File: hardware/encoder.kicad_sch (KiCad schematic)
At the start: 9 parts, among them SW2 PEC12R Encoder

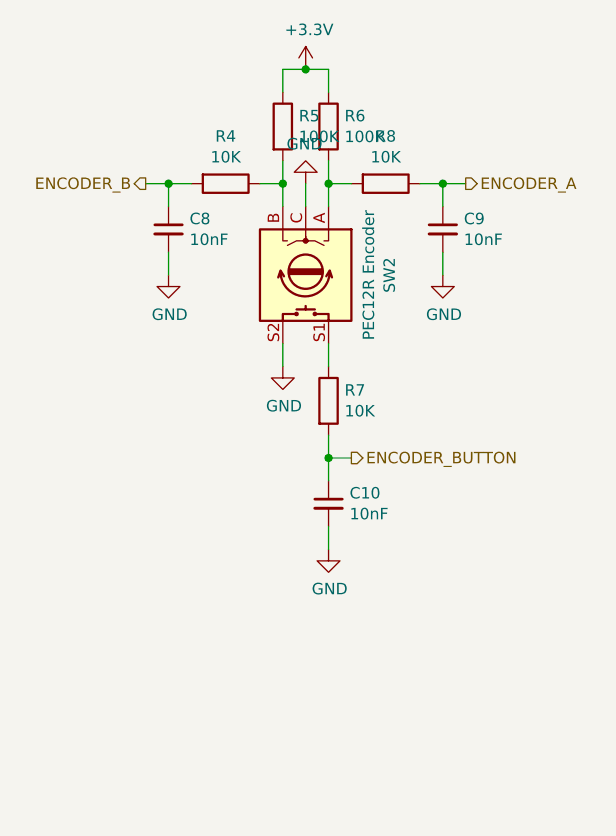
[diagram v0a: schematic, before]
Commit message: Updated schematic according to reference design
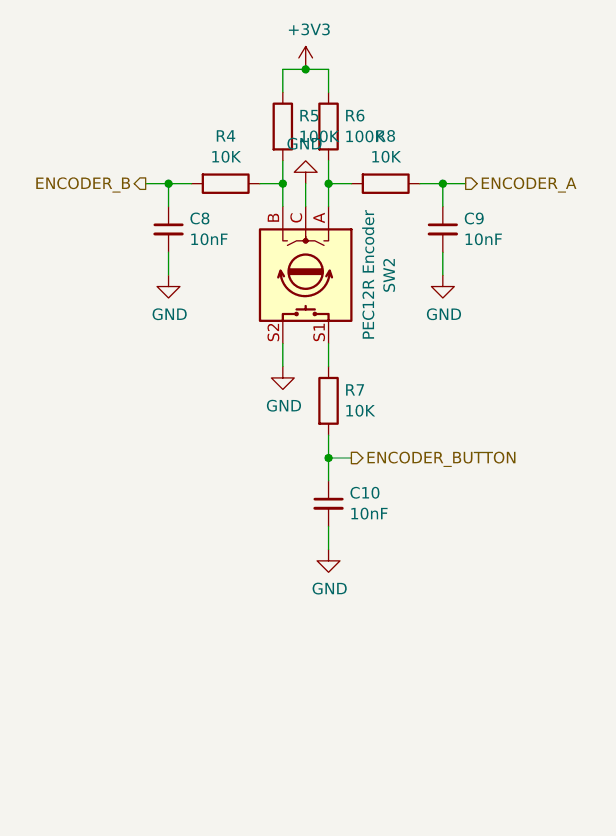
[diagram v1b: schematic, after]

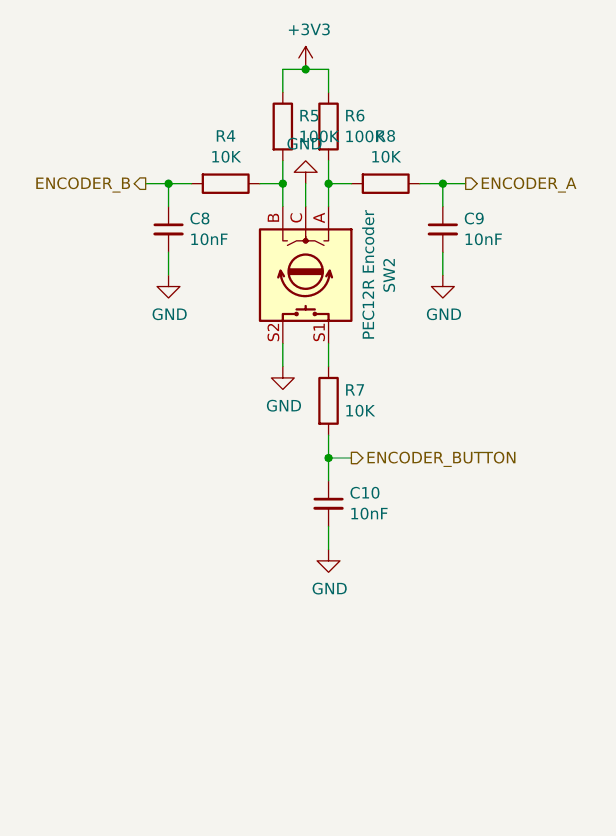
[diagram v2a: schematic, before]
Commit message: Regenerated reference designators, changed to rail-to-rail op-amps
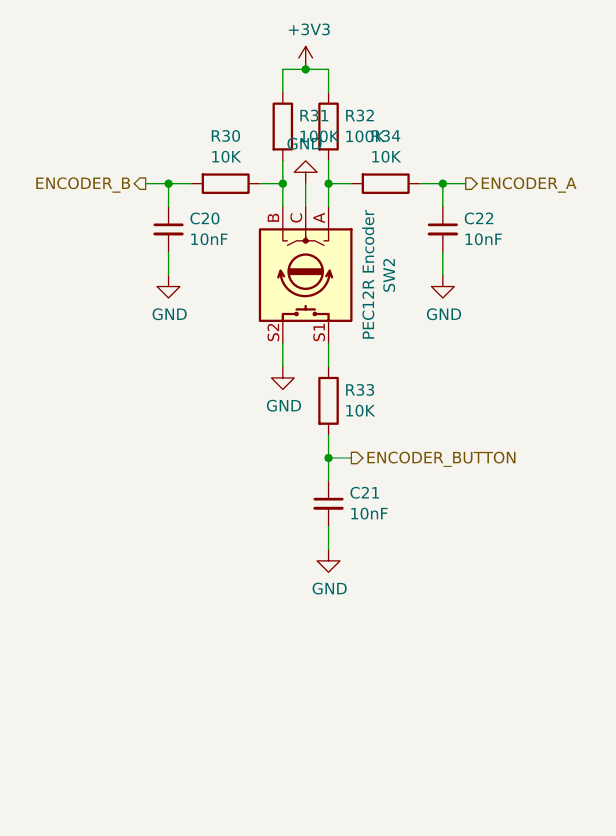
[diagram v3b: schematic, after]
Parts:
- renumbered C8 to C20, C10 to C21, C9 to C22, R4 to R30, R5 to R31, R6 to R32, R7 to R33, R8 to R34
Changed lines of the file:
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@@
 		(on_board yes)
 		(dnp no)
-		(property "Reference" "#PWR0109"
+		(property "Reference" "#PWR061"
 			(at 109.22 50.8 0)
 			(effects
@@
 			(project ""
 				(path "/adf38c8f-bada-4838-acc6-e6af19946742/82306041-d571-45f1-89c8-d149d0eff0c6"
-					(reference "#PWR0109")
+					(reference "#PWR061")
 					(unit 1)
 				)
@@
 		(on_board yes)
 		(dnp no)
-		(property "Reference" "R5"
+		(property "Reference" "R31"
 			(at 108.458 52.1716 0)
 			(effects
@@
 			(project ""
 				(path "/adf38c8f-bada-4838-acc6-e6af19946742/82306041-d571-45f1-89c8-d149d0eff0c6"
-					(reference "R5")
+					(reference "R31")
 					(unit 1)
 				)
@@
 		(on_board yes)
 		(dnp no)
-		(property "Reference" "R4"
+		(property "Reference" "R30"
 			(at 100.33 54.4322 90)
 			(effects
@@
 			(project ""
 				(path "/adf38c8f-bada-4838-acc6-e6af19946742/82306041-d571-45f1-89c8-d149d0eff0c6"
-					(reference "R4")
+					(reference "R30")
 					(unit 1)
 				)
@@
 		(on_board yes)
 		(dnp no)
-		(property "Reference" "R8"
+		(property "Reference" "R34"
 			(at 118.11 54.4322 90)
 			(effects
@@
 			(project ""
 				(path "/adf38c8f-bada-4838-acc6-e6af19946742/82306041-d571-45f1-89c8-d149d0eff0c6"
-					(reference "R8")
+					(reference "R34")
 					(unit 1)
 				)
@@
 		(on_board yes)
 		(dnp no)
-		(property "Reference" "R6"
+		(property "Reference" "R32"
 			(at 113.538 52.1716 0)
 			(effects
@@
 			(project ""
 				(path "/adf38c8f-bada-4838-acc6-e6af19946742/82306041-d571-45f1-89c8-d149d0eff0c6"
-					(reference "R6")
+					(reference "R32")
 					(unit 1)
 				)
@@
 		(on_board yes)
 		(dnp no)
-		(property "Reference" "R7"
+		(property "Reference" "R33"
 			(at 113.538 82.6516 0)
 			(effects
@@
 			(project ""
 				(path "/adf38c8f-bada-4838-acc6-e6af19946742/82306041-d571-45f1-89c8-d149d0eff0c6"
-					(reference "R7")
+					(reference "R33")
 					(unit 1)
 				)
@@
 		(on_board yes)
 		(dnp no)
-		(property "Reference" "C8"
+		(property "Reference" "C20"
 			(at 96.3168 63.6016 0)
 			(effects
@@
 			(project ""
 				(path "/adf38c8f-bada-4838-acc6-e6af19946742/82306041-d571-45f1-89c8-d149d0eff0c6"
-					(reference "C8")
+					(reference "C20")
 					(unit 1)
 				)
@@
 		(on_board yes)
 		(dnp no)
-		(property "Reference" "C9"
+		(property "Reference" "C22"
 			(at 126.7968 63.6016 0)
 			(effects
@@
 			(project ""
 				(path "/adf38c8f-bada-4838-acc6-e6af19946742/82306041-d571-45f1-89c8-d149d0eff0c6"
-					(reference "C9")
+					(reference "C22")
 					(unit 1)
 				)
@@
 		(on_board yes)
 		(dnp no)
-		(property "Reference" "#PWR0116"
+		(property "Reference" "#PWR060"
 			(at 106.68 86.36 0)
 			(effects
@@
 			(project ""
 				(path "/adf38c8f-bada-4838-acc6-e6af19946742/82306041-d571-45f1-89c8-d149d0eff0c6"
-					(reference "#PWR0116")
+					(reference "#PWR060")
 					(unit 1)
 				)
@@
 		(on_board yes)
 		(dnp no)
-		(property "Reference" "#PWR0117"
+		(property "Reference" "#PWR064"
 			(at 124.46 76.2 0)
 			(effects
@@
 			(project ""
 				(path "/adf38c8f-bada-4838-acc6-e6af19946742/82306041-d571-45f1-89c8-d149d0eff0c6"
-					(reference "#PWR0117")
+					(reference "#PWR064")
 					(unit 1)
 				)
@@
 		(on_board yes)
 		(dnp no)
-		(property "Reference" "#PWR0118"
+		(property "Reference" "#PWR059"
 			(at 93.98 76.2 0)
 			(effects
@@
 			(project ""
 				(path "/adf38c8f-bada-4838-acc6-e6af19946742/82306041-d571-45f1-89c8-d149d0eff0c6"
-					(reference "#PWR0118")
+					(reference "#PWR059")
 					(unit 1)
 				)
@@
 		(on_board yes)
 		(dnp no)
-		(property "Reference" "#PWR0119"
+		(property "Reference" "#PWR062"
 			(at 109.22 53.34 0)
 			(effects
@@
 			(project ""
 				(path "/adf38c8f-bada-4838-acc6-e6af19946742/82306041-d571-45f1-89c8-d149d0eff0c6"
-					(reference "#PWR0119")
+					(reference "#PWR062")
 					(unit 1)
 				)
@@
 		(on_board yes)
 		(dnp no)
-		(property "Reference" "C10"
+		(property "Reference" "C21"
 			(at 114.0968 94.0816 0)
 			(effects
@@
 			(project ""
 				(path "/adf38c8f-bada-4838-acc6-e6af19946742/82306041-d571-45f1-89c8-d149d0eff0c6"
-					(reference "C10")
+					(reference "C21")
 					(unit 1)
 				)
@@
 		(on_board yes)
 		(dnp no)
-		(property "Reference" "#PWR0136"
+		(property "Reference" "#PWR063"
 			(at 111.76 106.68 0)
 			(effects
@@
 			(project ""
 				(path "/adf38c8f-bada-4838-acc6-e6af19946742/82306041-d571-45f1-89c8-d149d0eff0c6"
-					(reference "#PWR0136")
-					(unit 1)
-				)
+					(reference "#PWR063")
+					(unit 1)
+				)

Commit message: Major changes to schematic
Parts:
- removed SW2: PEC12R Encoder, Custom:Bourns PEC12R Vertical, symbol Device:Rotary_Encoder_Switch
- added S1: PEC12R-3217F-S0024, custom:PEC12R3217FS0024, symbol PEC12R-3217F-S0024:PEC12R-3217F-S0024
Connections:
- net GND: now also S1.2 (NO), S1.C1 (COMMON), S1.MH1, S1.MH2
- net at R32.2, R34.2: now also S1.A1 (CHANNEL_A)
- net at R30.1, R31.2: now also S1.B1 (CHANNEL_B)
- net at R33.1: now also S1.1 (COM)
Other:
- moved on the sheet: C21, R33

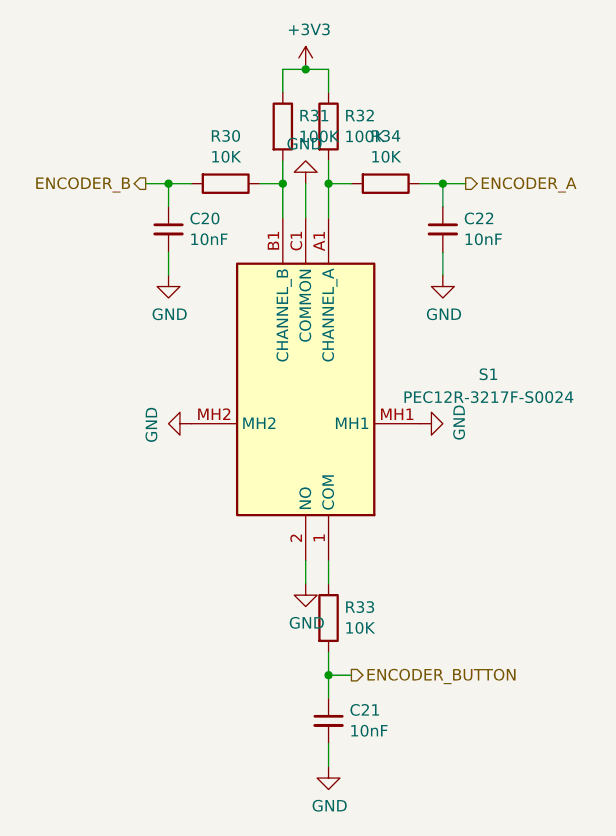
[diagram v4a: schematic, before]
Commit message: Fixed encoder and usb 3D models
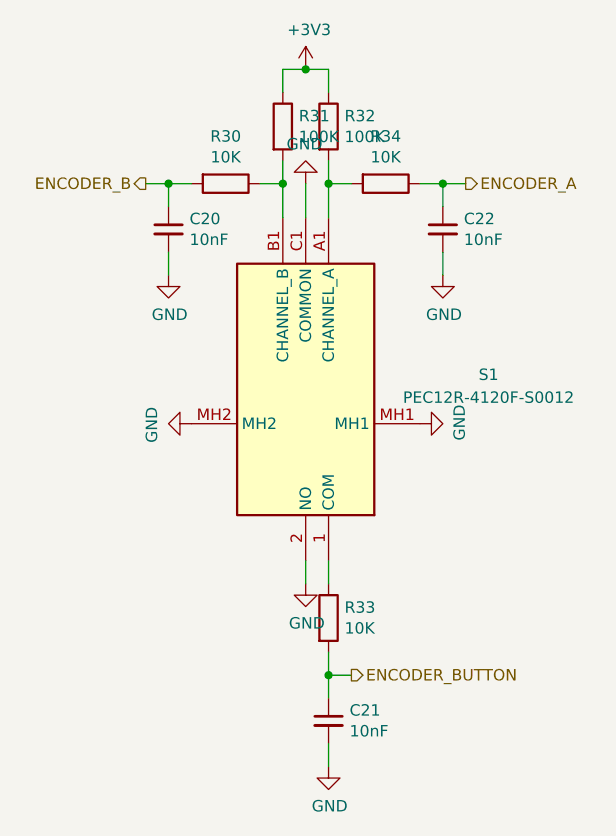
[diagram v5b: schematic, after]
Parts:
- S1: value PEC12R-3217F-S0024 -> PEC12R-4120F-S0012
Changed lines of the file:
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@@
 			)
 		)
-		(property "Value" "PEC12R-3217F-S0024"
+		(property "Value" "PEC12R-4120F-S0012"
 			(at 129.54 83.4546 0)
 			(effects
@@
 					(reference "S1")
 					(unit 1)
+				)
+				(path "/adf38c8f-bada-4838-acc6-e6af19946742/8a4812e6-01d2-4a59-bc73-706ba54f858f"
+					(reference "S1")
+					(unit 1)
